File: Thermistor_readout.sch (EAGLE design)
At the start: 25 parts, among them Q1 BC550C, U1 TI_NATIONAL_SEMICONDUCTOR_LF3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, U2 TI_NATIONAL_SEMICONDUCTOR_LF3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, U3 ANALOG_DEVICES_ADG725BSUZANAL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, U4 TI_NATIONAL_SEMICONDUCTOR_LF3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

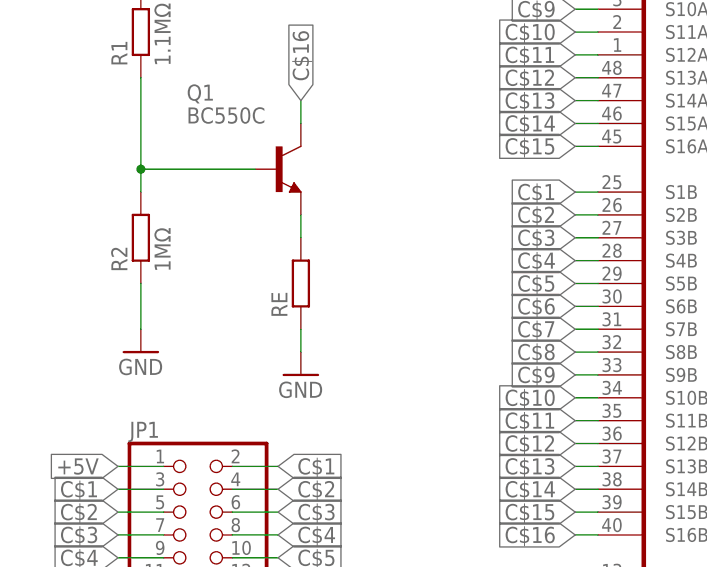
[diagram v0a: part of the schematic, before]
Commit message: double sized Re resistor
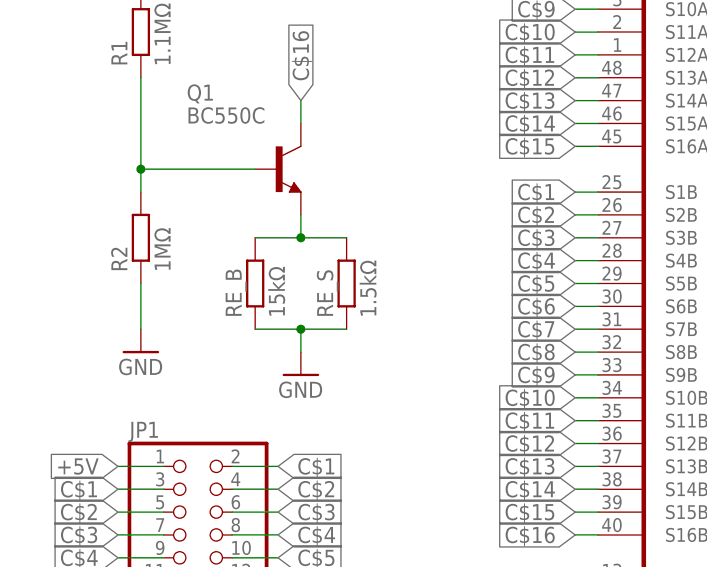
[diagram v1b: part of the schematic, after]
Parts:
- removed RE: (no value), 1AKarstenLib:R-EU_SMD0805H
- added RE_B: 15kΩ, 1AKarstenLib:R-EU_SMD1206H
- added RE_S: 1.5kΩ, 1AKarstenLib:R-EU_SMD0805H
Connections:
- net GND: now also RE_B.1, RE_S.1; no longer RE.1
- net N$2: now also RE_B.2, RE_S.2; no longer RE.2
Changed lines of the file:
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@@
 <layers>
 <layer number="1" name="Top" color="4" fill="1" visible="no" active="no"/>
+<layer number="2" name="Route2" color="1" fill="3" visible="no" active="no"/>
+<layer number="3" name="Route3" color="4" fill="3" visible="no" active="no"/>
+<layer number="4" name="Route4" color="1" fill="4" visible="no" active="no"/>
+<layer number="5" name="Route5" color="4" fill="4" visible="no" active="no"/>
+<layer number="6" name="Route6" color="1" fill="8" visible="no" active="no"/>
+<layer number="7" name="Route7" color="4" fill="8" visible="no" active="no"/>
+<layer number="8" name="Route8" color="1" fill="2" visible="no" active="no"/>
+<layer number="9" name="Route9" color="4" fill="2" visible="no" active="no"/>
+<layer number="10" name="Route10" color="1" fill="7" visible="no" active="no"/>
+<layer number="11" name="Route11" color="4" fill="7" visible="no" active="no"/>
+<layer number="12" name="Route12" color="1" fill="5" visible="no" active="no"/>
+<layer number="13" name="Route13" color="4" fill="5" visible="no" active="no"/>
+<layer number="14" name="Route14" color="1" fill="6" visible="no" active="no"/>
+<layer number="15" name="Route15" color="4" fill="6" visible="no" active="no"/>
 <layer number="16" name="Bottom" color="1" fill="1" visible="no" active="no"/>
 <layer number="17" name="Pads" color="2" fill="1" visible="no" active="no"/>
@@
 <part name="C11" library="1AKarstenLib" deviceset="C-EU_SMD" device="C1206H/D"/>
 <part name="CON1" library="con-harting" deviceset="CON16L" device=""/>
-<part name="RE" library="1AKarstenLib" deviceset="R-EU_SMD" device="0805H"/>
+<part name="RE_B" library="1AKarstenLib" deviceset="R-EU_SMD" device="1206H" value="15kΩ"/>
+<part name="RE_S" library="1AKarstenLib" deviceset="R-EU_SMD" device="0805H" value="1.5kΩ"/>
 </parts>
 <sheets>
@@
 <instance part="C11" gate="G$1" x="162.56" y="25.4"/>
 <instance part="CON1" gate="G$1" x="185.42" y="25.4"/>
-<instance part="RE" gate="G$1" x="53.34" y="71.12" rot="R90"/>
+<instance part="RE_B" gate="G$1" x="48.26" y="71.12" rot="R90"/>
+<instance part="RE_S" gate="G$1" x="58.42" y="71.12" rot="R90"/>
 </instances>
 <busses>
@@
 <pinref part="Q1" gate="G$1" pin="E"/>
 <wire x1="53.34" y1="78.74" x2="53.34" y2="76.2" width="0.1524" layer="91"/>
-<pinref part="RE" gate="G$1" pin="2"/>
+<pinref part="RE_B" gate="G$1" pin="2"/>
+<wire x1="48.26" y1="76.2" x2="53.34" y2="76.2" width="0.1524" layer="91"/>
+<pinref part="RE_S" gate="G$1" pin="2"/>
+<wire x1="53.34" y1="76.2" x2="58.42" y2="76.2" width="0.1524" layer="91"/>
+<junction x="53.34" y="76.2"/>
 </segment>
 </net>
@@
 <pinref part="GND3" gate="1" pin="GND"/>
 <wire x1="53.34" y1="66.04" x2="53.34" y2="63.5" width="0.1524" layer="91"/>
-<pinref part="RE" gate="G$1" pin="1"/>
-</segment>
-<segment>
+<pinref part="RE_B" gate="G$1" pin="1"/>
+<wire x1="48.26" y1="66.04" x2="53.34" y2="66.04" width="0.1524" layer="91"/>
+<pinref part="RE_S" gate="G$1" pin="1"/>
+<wire x1="53.34" y1="66.04" x2="58.42" y2="66.04" width="0.1524" layer="91"/>
+<junction x="53.34" y="66.04"/>
+</segment>
+<segment>

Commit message: 1206_capacitors
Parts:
- C1, C2, C3, C4, C5, C6, C7, C8: device 1AKarstenLib:C-EU_SMDR0805H -> 1AKarstenLib:C-EU_SMDR1206H
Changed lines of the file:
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@@
 <part name="GND7" library="supply1" deviceset="GND" device=""/>
 <part name="U3" library="Analog Devices - ADG725BSUZ" deviceset="ANALOG_DEVICES_ADG725BSUZ" device="ANALOG_DEVICES_ADG725BSUZ_0_2"/>
-<part name="C1" library="1AKarstenLib" deviceset="C-EU_SMD" device="R0805H"/>
-<part name="C2" library="1AKarstenLib" deviceset="C-EU_SMD" device="R0805H"/>
-<part name="C3" library="1AKarstenLib" deviceset="C-EU_SMD" device="R0805H"/>
-<part name="C4" library="1AKarstenLib" deviceset="C-EU_SMD" device="R0805H"/>
+<part name="C1" library="1AKarstenLib" deviceset="C-EU_SMD" device="R1206H"/>
+<part name="C2" library="1AKarstenLib" deviceset="C-EU_SMD" device="R1206H"/>
+<part name="C3" library="1AKarstenLib" deviceset="C-EU_SMD" device="R1206H"/>
+<part name="C4" library="1AKarstenLib" deviceset="C-EU_SMD" device="R1206H"/>
 <part name="GND5" library="supply1" deviceset="GND" device=""/>
 <part name="GND8" library="supply1" deviceset="GND" device=""/>
@@
 <part name="GND10" library="supply1" deviceset="GND" device=""/>
 <part name="U1" library="TI National Semiconductor - LF356M" deviceset="TI_NATIONAL_SEMICONDUCTOR_LF356M" device="TI_NATIONAL_SEMICONDUCTOR_LF356M_0_2"/>
-<part name="C5" library="1AKarstenLib" deviceset="C-EU_SMD" device="R0805H"/>
-<part name="C6" library="1AKarstenLib" deviceset="C-EU_SMD" device="R0805H"/>
+<part name="C5" library="1AKarstenLib" deviceset="C-EU_SMD" device="R1206H"/>
+<part name="C6" library="1AKarstenLib" deviceset="C-EU_SMD" device="R1206H"/>
 <part name="GND11" library="supply1" deviceset="GND" device=""/>
 <part name="GND12" library="supply1" deviceset="GND" device=""/>
@@
 <part name="P-7" library="supply1" deviceset="-15V" device=""/>
 <part name="U4" library="TI National Semiconductor - LF356M" deviceset="TI_NATIONAL_SEMICONDUCTOR_LF356M" device="TI_NATIONAL_SEMICONDUCTOR_LF356M_0_2"/>
-<part name="C7" library="1AKarstenLib" deviceset="C-EU_SMD" device="R0805H"/>
-<part name="C8" library="1AKarstenLib" deviceset="C-EU_SMD" device="R0805H"/>
+<part name="C7" library="1AKarstenLib" deviceset="C-EU_SMD" device="R1206H"/>
+<part name="C8" library="1AKarstenLib" deviceset="C-EU_SMD" device="R1206H"/>
 <part name="GND13" library="supply1" deviceset="GND" device=""/>
 <part name="P+3" library="supply1" deviceset="+15V" device=""/>

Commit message: production
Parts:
- removed U2: TI_NATIONAL_SEMICONDUCTOR_LF356MTI_NATIONAL_SEMICONDUCTOR_L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, TI National Semiconductor - LF356M:TI_NATIONAL_SEMICONDUCTOR_LF356MTI_NATIONAL_SEMICONDUCTOR_LF356M_0_2
- added TP1VIN, TP1VOUT, TP2VIN, TP2VOUT, TP3V+, TP3V-, TP3VOUT, TPGND, TPVB, TPVC, TPVE: PTR1TP20R, testpad:PTR1TP20R
- added U: ANALOG_DEVICES_ADG725BSUZANALOG_DEVICES_ADG725BSUZ_0_2, Analog Devices - ADG725BSUZ:ANALOG_DEVICES_ADG725BSUZANALOG_DEVICES_ADG725BSUZ_0_2
- U3: value ANALOG_DEVICES_ADG725BSUZANALOG_DEVICES_ADG725BSUZ_0_2 -> TI_NATIONAL_SEMICONDUCTOR_LF356MTI_NATIONAL_SEMICONDUCTOR_LF356M_0_2; device Analog Devices - ADG725BSUZ:ANALOG_DEVICES_ADG725BSUZANALOG_DEVICES_ADG725BSUZ_0_2 -> TI National Semiconductor - LF356M:TI_NATIONAL_SEMICONDUCTOR_LF356MTI_NATIONAL_SEMICONDUCTOR_LF356M_0_2
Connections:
- net +15V: now also U3.V+; no longer U2.V+
- net +5V: now also U.1_VDD, U.2_VDD, U.S1A; no longer U3.1_VDD, U3.2_VDD, U3.S1A
- net -15V: now also U3.V-; no longer U2.V-
- net C$1: now also U.S1B, U.S2A; no longer U3.S1B, U3.S2A
- net C$10: now also U.S10B, U.S11A; no longer U3.S10B, U3.S11A
- net C$11: now also U.S11B, U.S12A; no longer U3.S11B, U3.S12A
- net C$12: now also U.S12B, U.S13A; no longer U3.S12B, U3.S13A
- net C$13: now also U.S13B, U.S14A; no longer U3.S13B, U3.S14A
- net C$14: now also U.S14B, U.S15A; no longer U3.S14B, U3.S15A
- net C$15: now also U.S15B, U.S16A; no longer U3.S15B, U3.S16A
- net C$16: now also TPVC.TP, U.S16B; no longer U3.S16B
- net C$2: now also U.S2B, U.S3A; no longer U3.S2B, U3.S3A
- net C$3: now also U.S3B, U.S4A; no longer U3.S3B, U3.S4A
- net C$4: now also U.S4B, U.S5A; no longer U3.S4B, U3.S5A
- net C$5: now also U.S5B, U.S6A; no longer U3.S5B, U3.S6A
- net C$6: now also U.S6B, U.S7A; no longer U3.S6B, U3.S7A
- net C$7: now also U.S7B, U.S8A; no longer U3.S7B, U3.S8A
- net C$8: now also U.S8B, U.S9A; no longer U3.S8B, U3.S9A
- net C$9: now also U.S10A, U.S9B; no longer U3.S10A, U3.S9B
- net GND: now also TPGND.TP, U.GND, U.VSS; no longer U3.GND, U3.VSS
- net N$1: now also TPVB.TP
- net N$11: now also U.SCLK; no longer U3.SCLK
- net N$13: now also U.!SYNC!; no longer U3.!SYNC!
- net N$14: now also U.DIN; no longer U3.DIN
- net N$2: now also TPVE.TP
- net N$24: now also TP3VOUT.TP, U3.OUT; no longer U2.OUT
- net N$3: now also TP2VIN.TP, U.DB; no longer U3.DB
- net N$4: now also TP1VOUT.TP
- net N$5: now also TP3V-.TP, U3.IN-; no longer U2.IN-
- net N$6: now also TP3V+.TP, U3.IN+; no longer U2.IN+
- net N$7: now also TP1VIN.TP, U.DA; no longer U3.DA
- net N$8: now also TP2VOUT.TP
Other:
- note added: "Srylab 05/2022 Thermistors Readout v1.0 Jacopo De Santis"
- note removed: "Srylab 02/2022 Thermistors Readout v1.0 Jacopo De Santis"
